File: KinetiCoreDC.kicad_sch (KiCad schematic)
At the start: 15 parts, among them J2 TC2070-IDC-NL, Q1 BSN20, Q2 BSN20, U1 STM32G070KBT6, U10 MCP1703Ax-330xxDB, U3 DRV8874PWPR, U9 LTC4365TS8

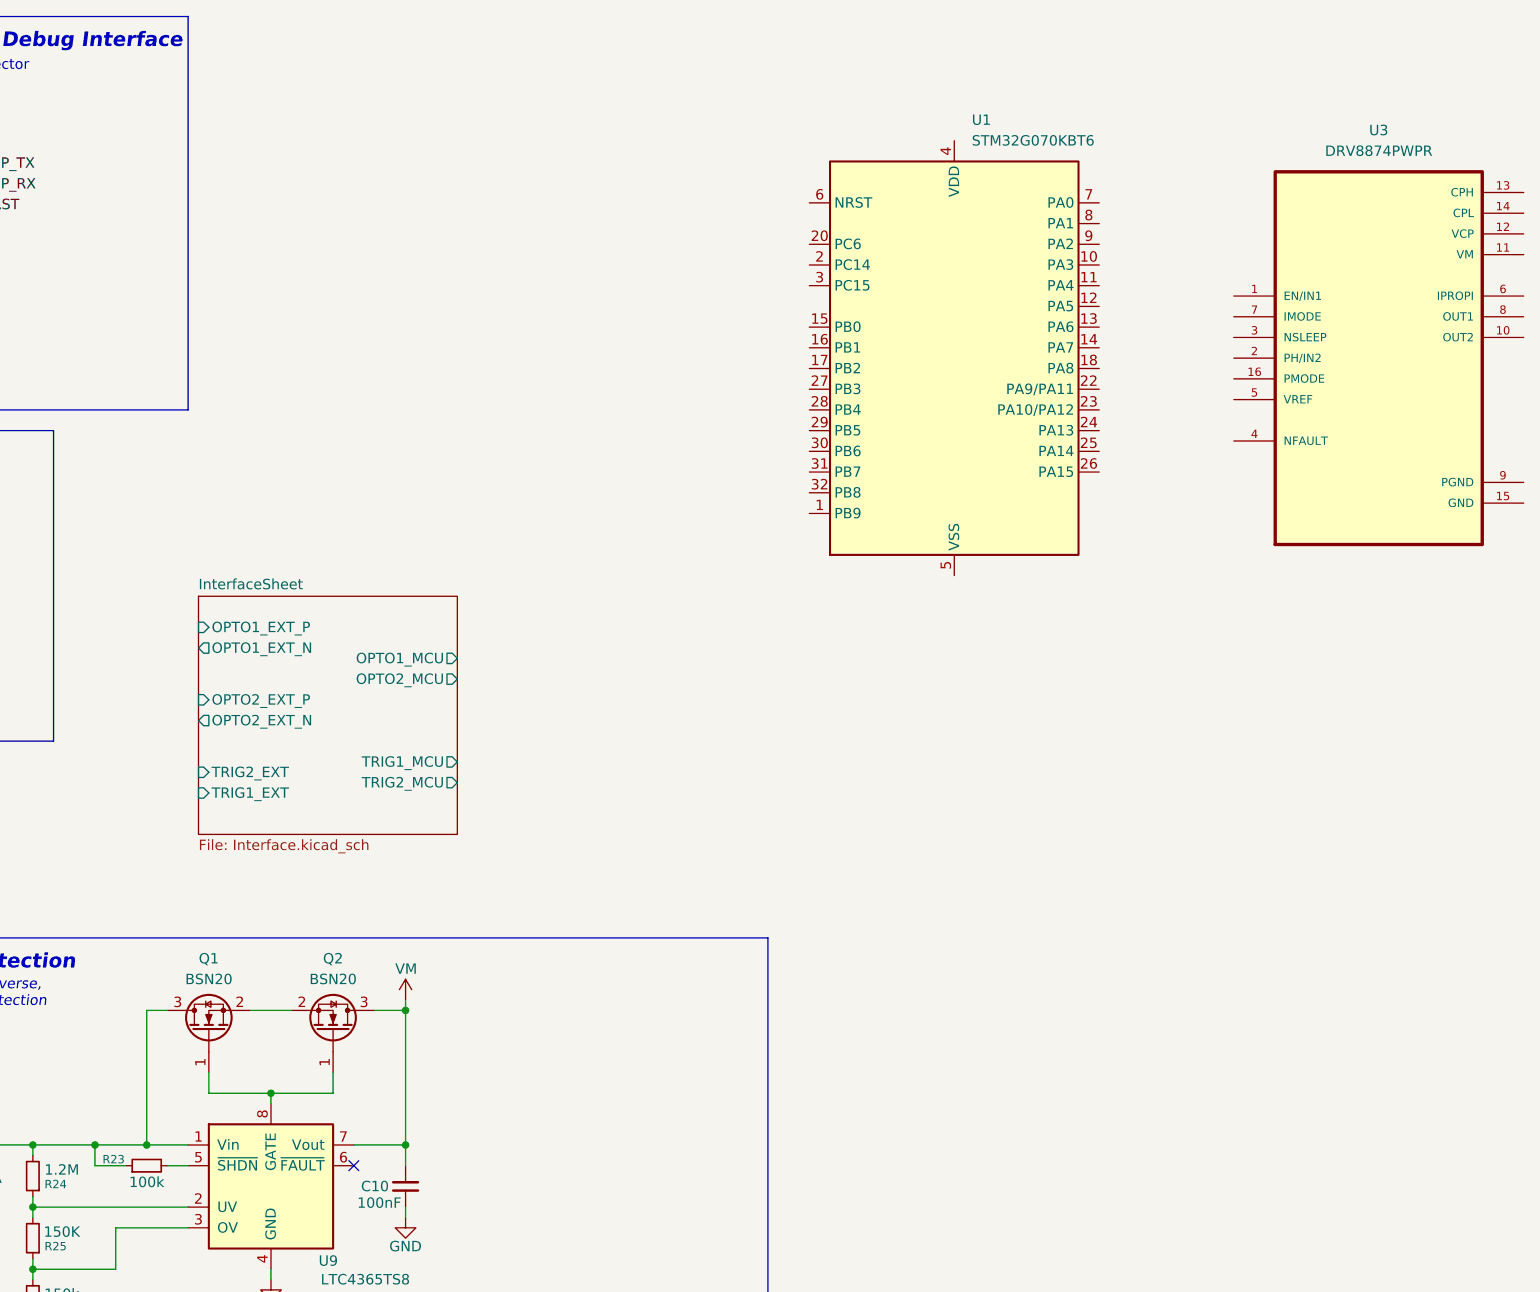
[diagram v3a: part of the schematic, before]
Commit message: feat: add driver component and some correction
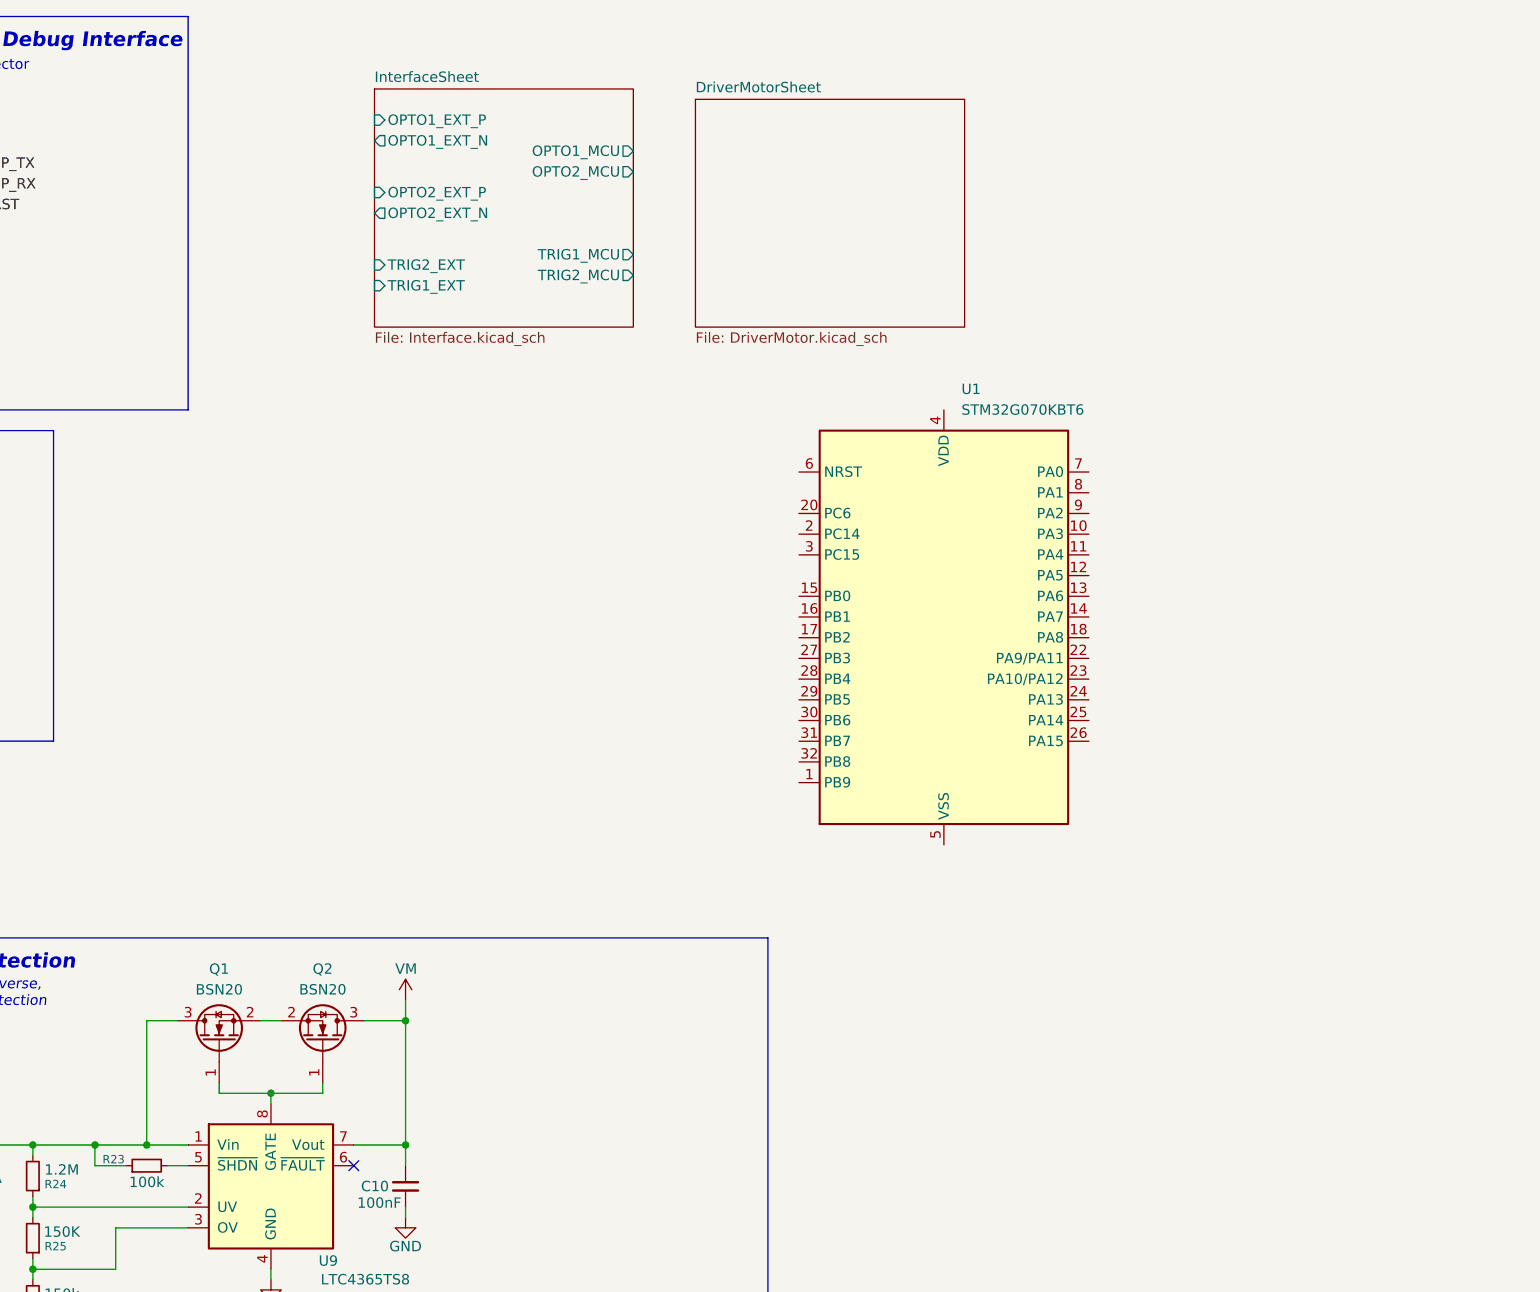
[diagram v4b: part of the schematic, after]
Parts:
- removed U3: DRV8874PWPR, KineticCore:SOP65P640X120-17N, symbol KineticCore:DRV8874PWPR
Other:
- added sheet DriverMotorSheet (DriverMotor.kicad_sch)
- moved on the sheet: Q1, Q2, U1

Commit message: feat: integrate DRV8874 H-bridge stage with current sensing and polarity LEDs
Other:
- title: KinetiCoreDC -> KinetiCoreDC - Main
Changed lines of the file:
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@@
 	(paper "A4")
 	(title_block
-		(title "KinetiCoreDC")
+		(title "KinetiCoreDC - Main")
 		(date "2026-10-09")
 		(rev "V°1")

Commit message: feat(hw): add asymmetrical RC pulse stretcher for UART TX/RX activity LEDs
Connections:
- net VIN: now reaches D6.1 (A1), Q1.3 (D), R23.1, R24.2, U9.1 (Vin)
- no-connect marks 6 -> 5
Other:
- note added: "Overvoltage, Undervoltage, Reverse, and ESD Input Protection"
- note removed: "Overvoltage, Undervoltage, Reverse, Overcurrent and ESD Input Protection"
- moved on the sheet: C10, C13, C14, U10

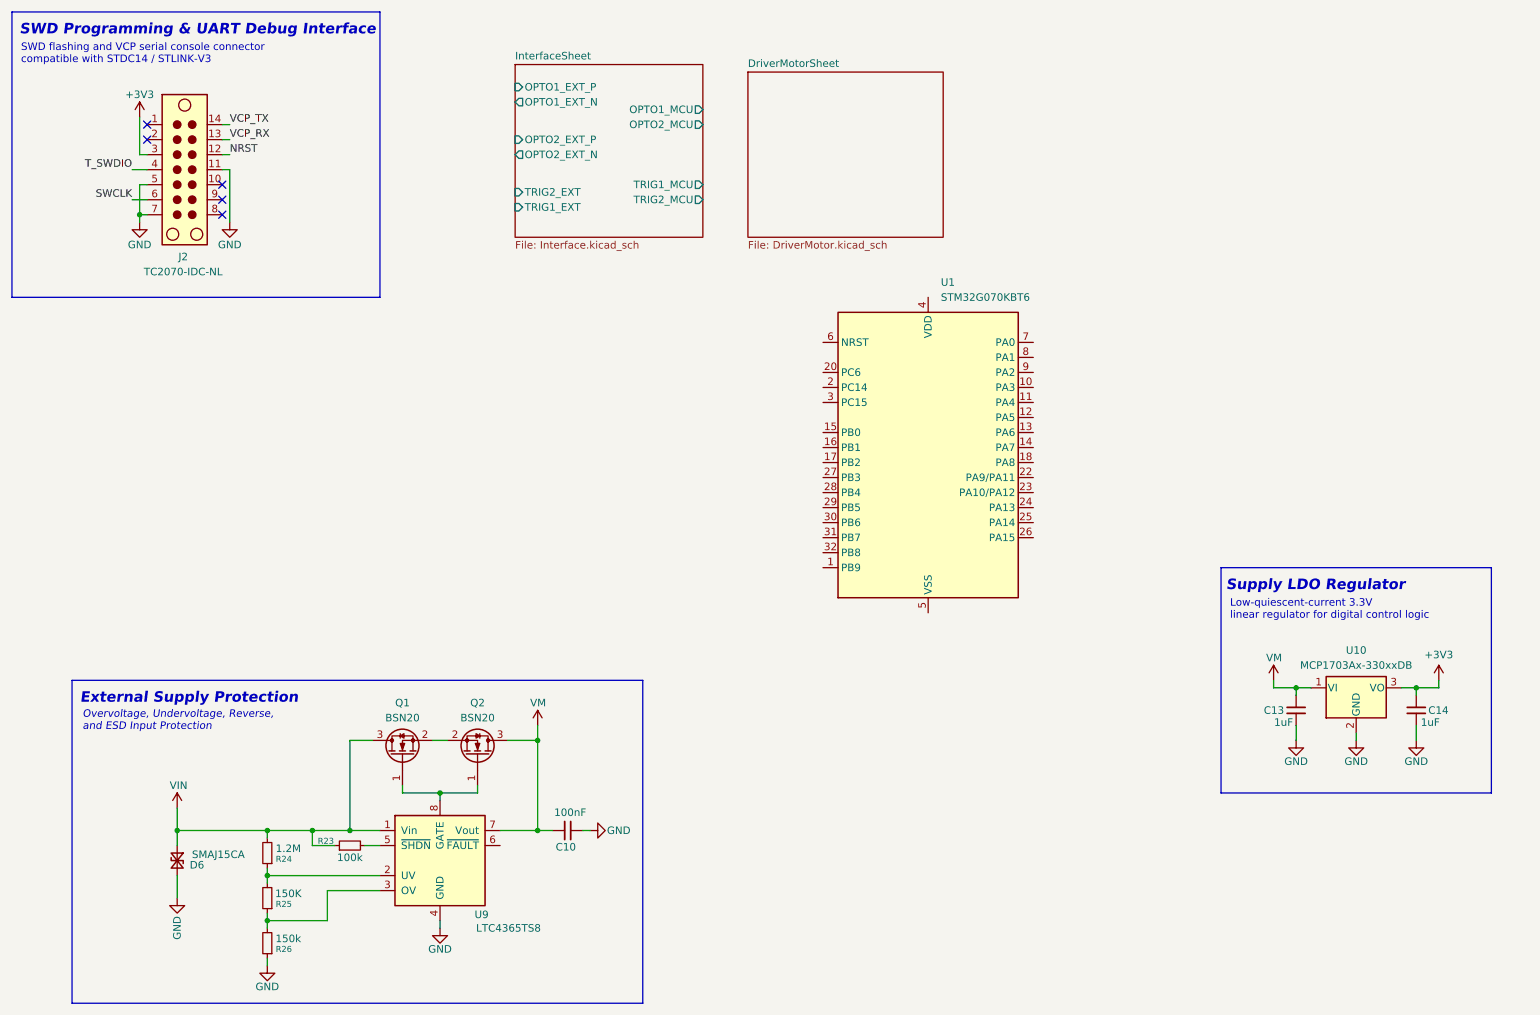
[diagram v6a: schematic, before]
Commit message: feat:add power sheat
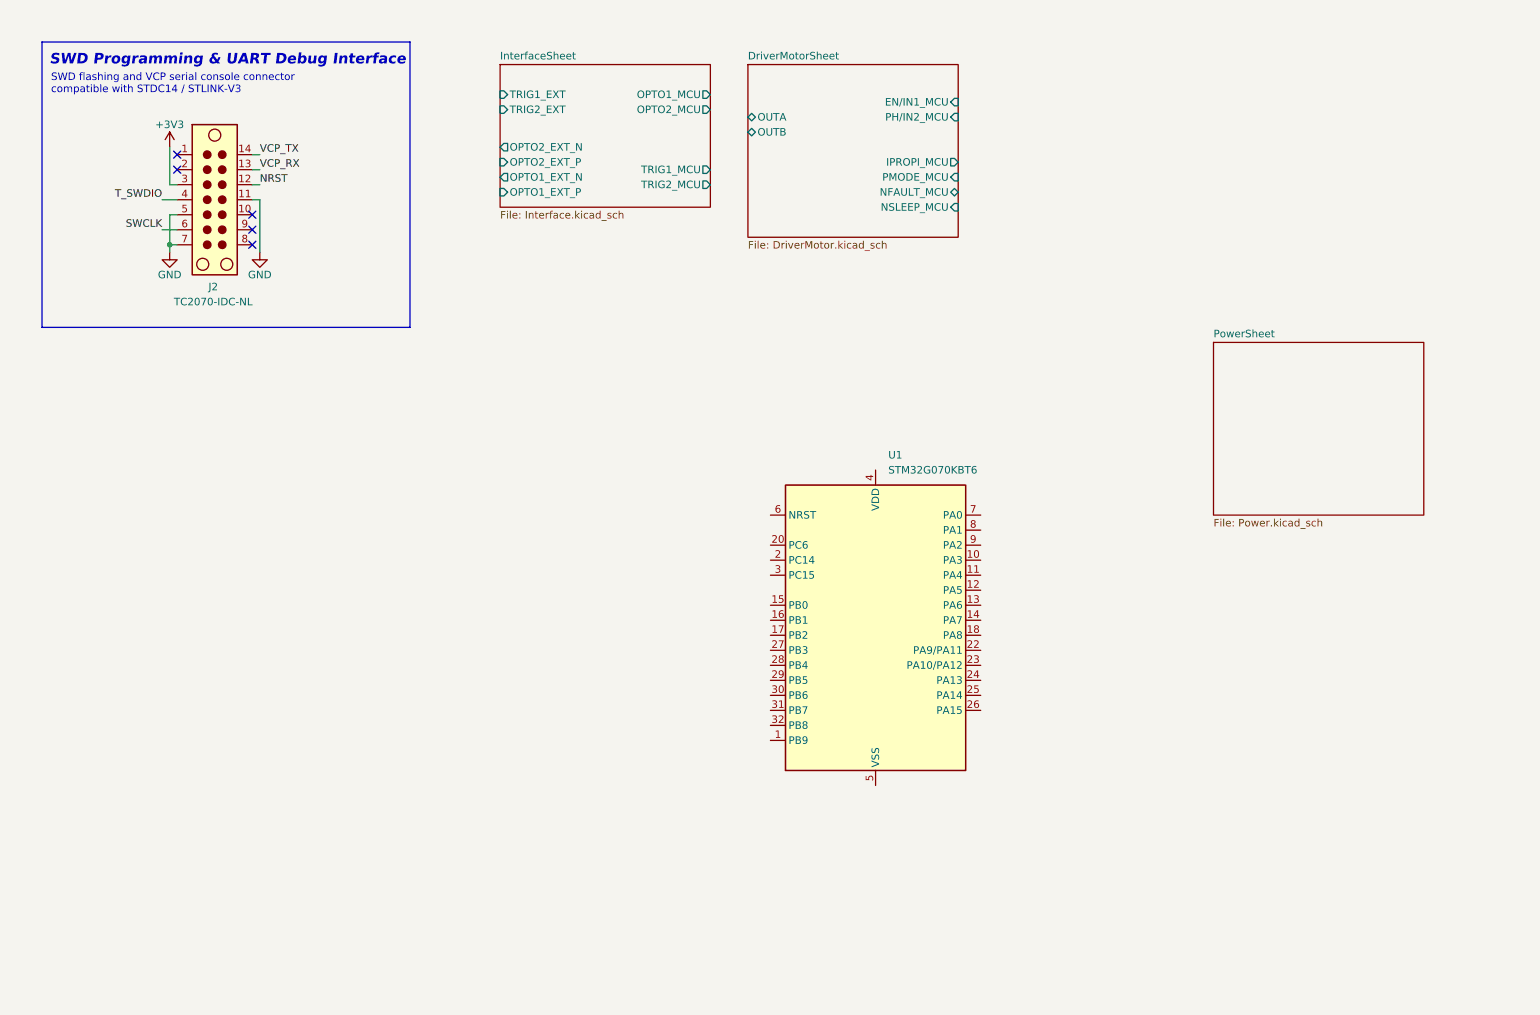
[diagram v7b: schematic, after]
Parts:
- removed C10: 100nF, Capacitor_SMD:C_0603_1608Metric, symbol Device:C_Small
- removed C13, C14: 1uF, Capacitor_SMD:C_0603_1608Metric, symbol Device:C_Small
- removed D6: SMAJ15CA, Diode_SMD:D_SMA, symbol Device:D_TVS_Small
- removed Q1, Q2: BSN20, Package_TO_SOT_SMD:SOT-23, symbol Transistor_FET:BSN20
- removed R23: 100k, Resistor_SMD:R_0603_1608Metric, symbol Device:R_Small
- removed R24: 1.2M, Resistor_SMD:R_0603_1608Metric, symbol Device:R_Small
- removed R25: 150K, Resistor_SMD:R_0603_1608Metric, symbol Device:R_Small
- removed R26: 150k, Resistor_SMD:R_0603_1608Metric, symbol Device:R_Small
- removed U10: MCP1703Ax-330xxDB, Package_TO_SOT_SMD:SOT-223-3_TabPin2, symbol Regulator_Linear:MCP1703Ax-330xxDB
- removed U9: LTC4365TS8, Package_TO_SOT_SMD:TSOT-23-8, symbol Power_Management:LTC4365TS8
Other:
- added sheet PowerSheet (Power.kicad_sch)
- sheet DriverMotorSheet ports: added EN/IN1_MCU, IPROPI_MCU, NFAULT_MCU, NSLEEP_MCU, OUTA, OUTB, PH/IN2_MCU, PMODE_MCU; removed none
- note removed: "External Supply Protection"
- note removed: "Low-quiescent-current 3.3V linear regulator for digital control logic"
- note removed: "Overvoltage, Undervoltage, Reverse, and ESD Input Protection"
- note removed: "Supply LDO Regulator"
- moved on the sheet: J2, U1

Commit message: feat: add quadrature encoder interface
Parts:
- added C10, C22: 100nF, Capacitor_SMD:C_0603_1608Metric, symbol Device:C_Small
- added C23: 4.7uF, Capacitor_SMD:C_0603_1608Metric, symbol Device:C_Small
- added R23: 100R, Resistor_SMD:R_0603_1608Metric, symbol Device:R_Small
- added SW1: PTS647, Button_Switch_SMD:SW_SPST_PTS647_Sx38, symbol Switch:SW_Push
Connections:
- net T_SWDIO is gone; now on net SWDIO: J2.4
- net GND: now also U1.5 (VSS), C10.2, C22.2, C23.2, SW1.1
- net NRST: now also R23.1
- net SWCLK: now also U1.25 (PA14)
- net USART2_RX: now reaches U1.10 (PA3)
- net SWDIO: now reaches U1.24 (PA13)
- net +3.3V: now reaches U1.4 (VDD)
- net +3.3V: now also C22.1, C23.1
- net at U1.6 (NRST): now also C10.1, R23.2, SW1.2
- net USART2_DE: now reaches U1.8 (PA1)
- net USART2_TX: now reaches U1.9 (PA2)
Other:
- moved on the sheet: U1
